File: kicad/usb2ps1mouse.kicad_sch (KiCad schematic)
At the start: 14 parts, among them J1 Conn_01x07_Pin, J2 Conn_01x01_Pin, J3 Conn_01x01_Pin, J4 USB_A, U2 ME2108A50PG

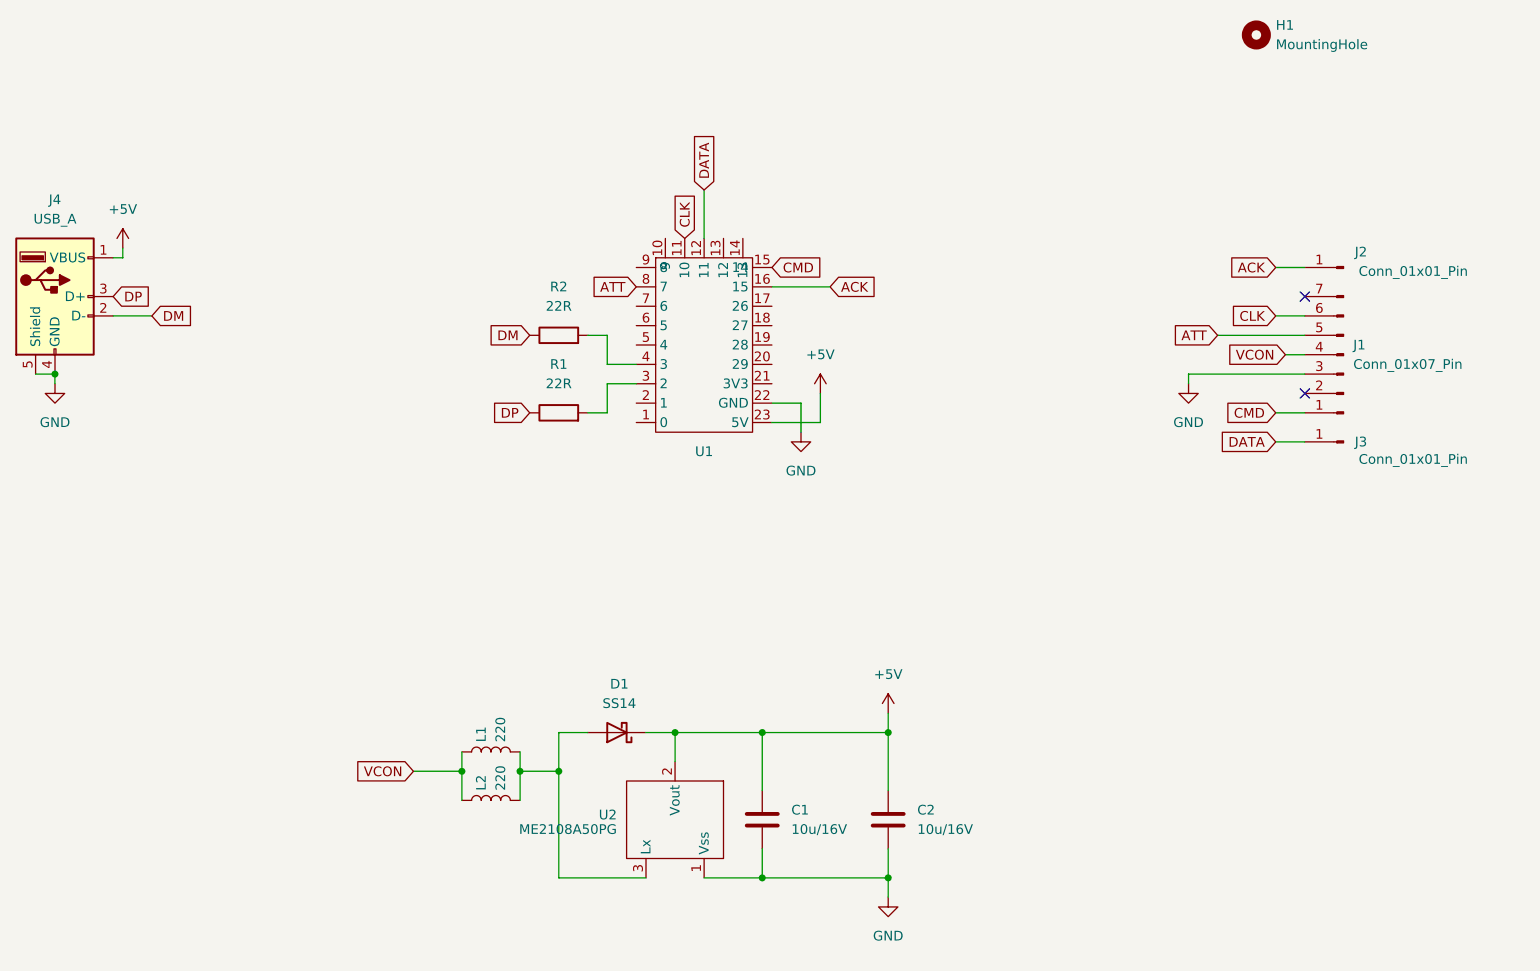
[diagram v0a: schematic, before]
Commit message: Update schematic
Add BOM
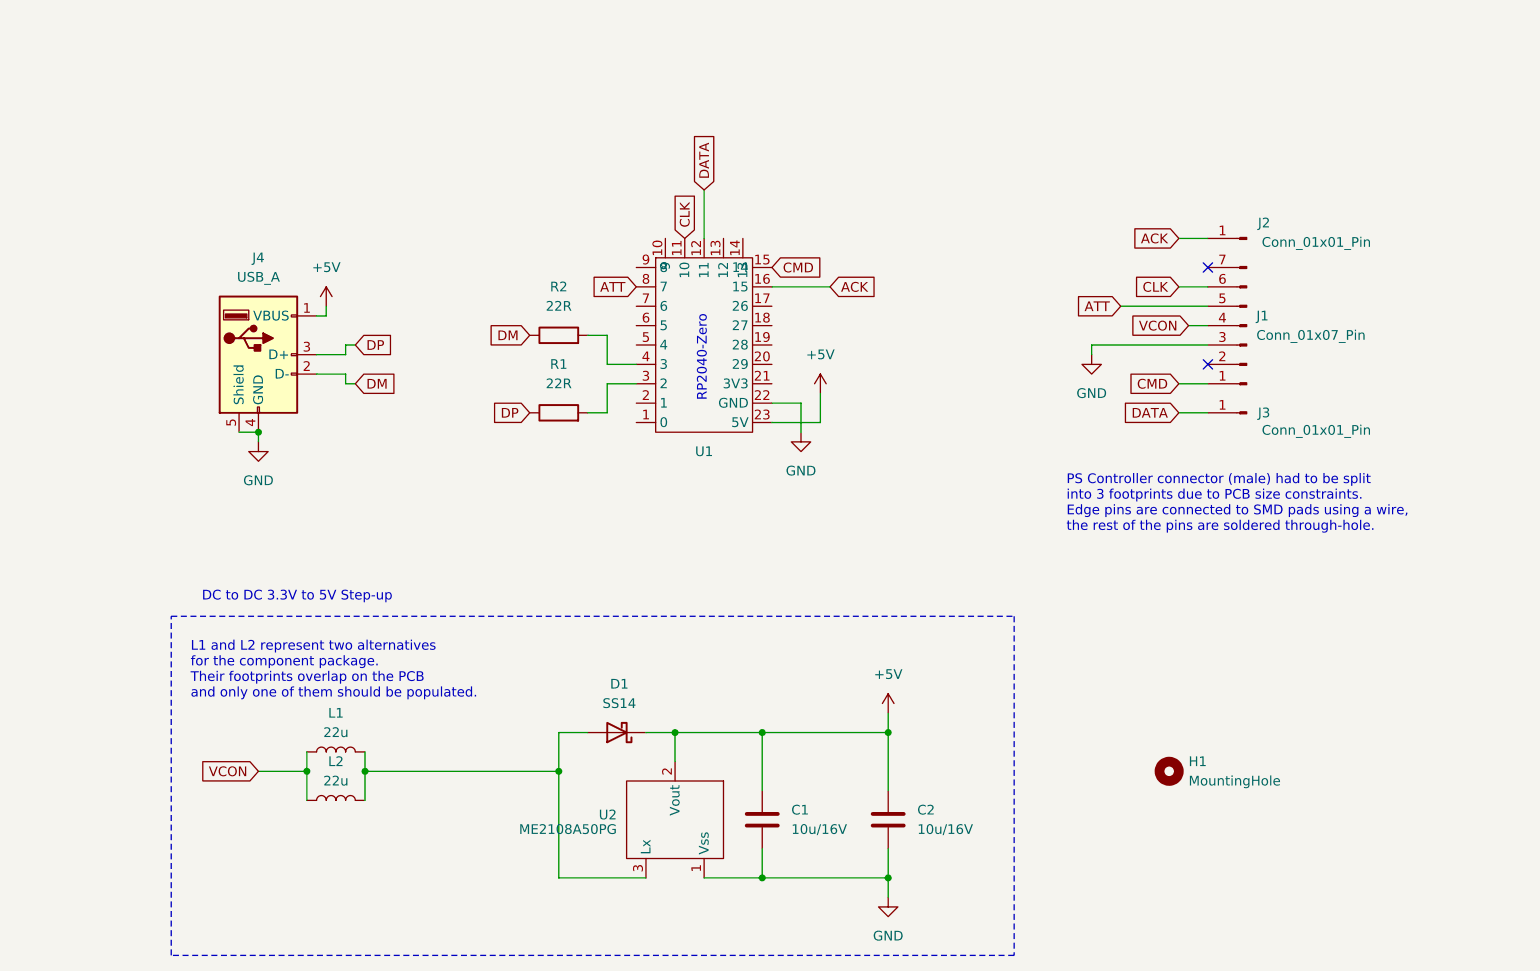
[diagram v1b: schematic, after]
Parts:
- L1, L2: value 220 -> 22u
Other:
- note added: "DC to DC 3.3V to 5V Step-up"
- note added: "L1 and L2 represent two alternatives for the component package. Their footprints overlap on the PCB and only one of them should be populated."
- note added: "PS Controller connector (male) had to be split into 3 footprints due to PCB size constraints. Edge pins are connected to SMD pads using a wire, the rest of the pins are soldered through-hole."
- note added: "RP2040-Zero"
- company: (none) -> Franticware
- title: (none) -> usb-to-ps1-mouse-pro schematic
- moved on the sheet: H1, J1, J2, J3, J4, L1, L2
